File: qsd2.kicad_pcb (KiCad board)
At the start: 2 copper layers, 100 x 75 mm, 65 parts, among them J1 5-1814832-1, J2 5-1814832-1, J3 Conn_02x08_Odd_Even, J4 SJ-3524-SMT, U1 SN74LVC1G14DBV, U10 GALI-39, U2 SN74LVC1G14DBV, U3 SN74CBT3253, U4 SN74AC74PW, U5 AD8226ARZ-R7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

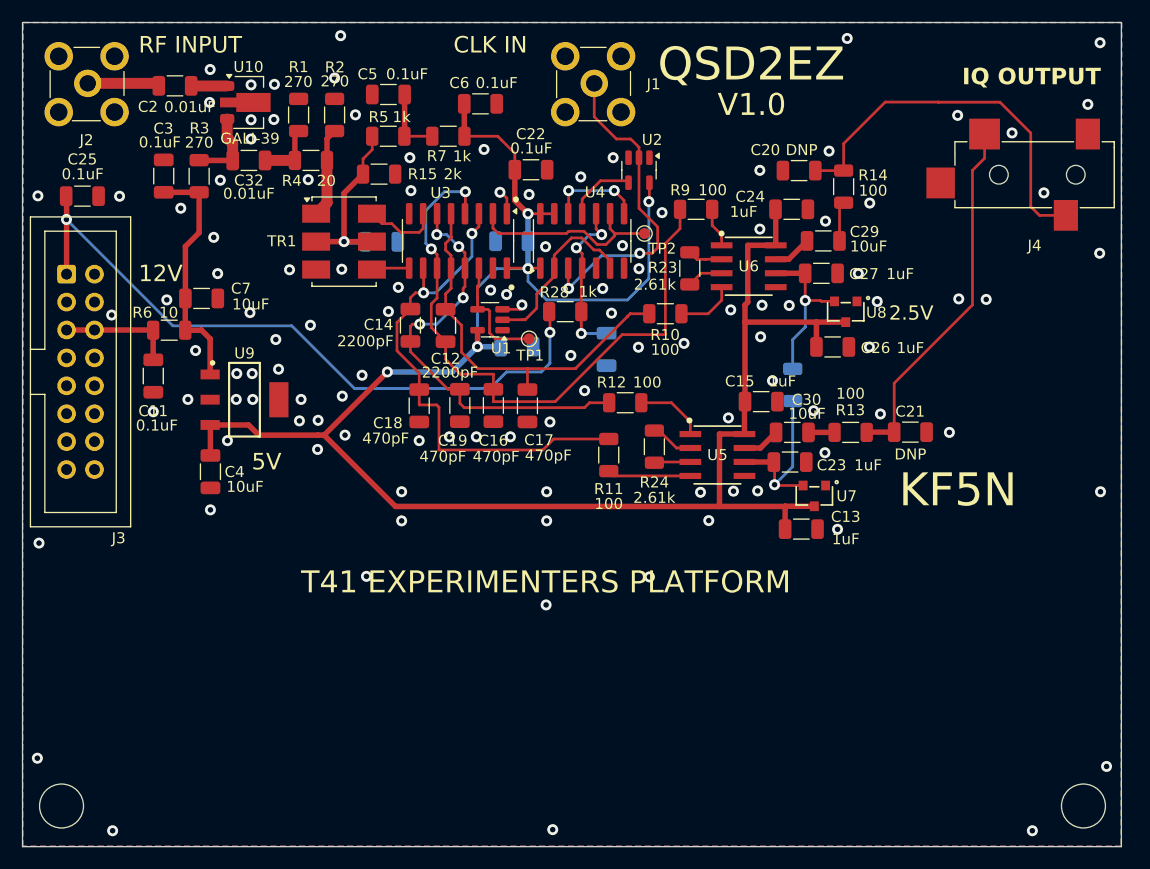
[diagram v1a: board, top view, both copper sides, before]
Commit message: Added 4 pin connector with 5V and I2C for Si5351 module.
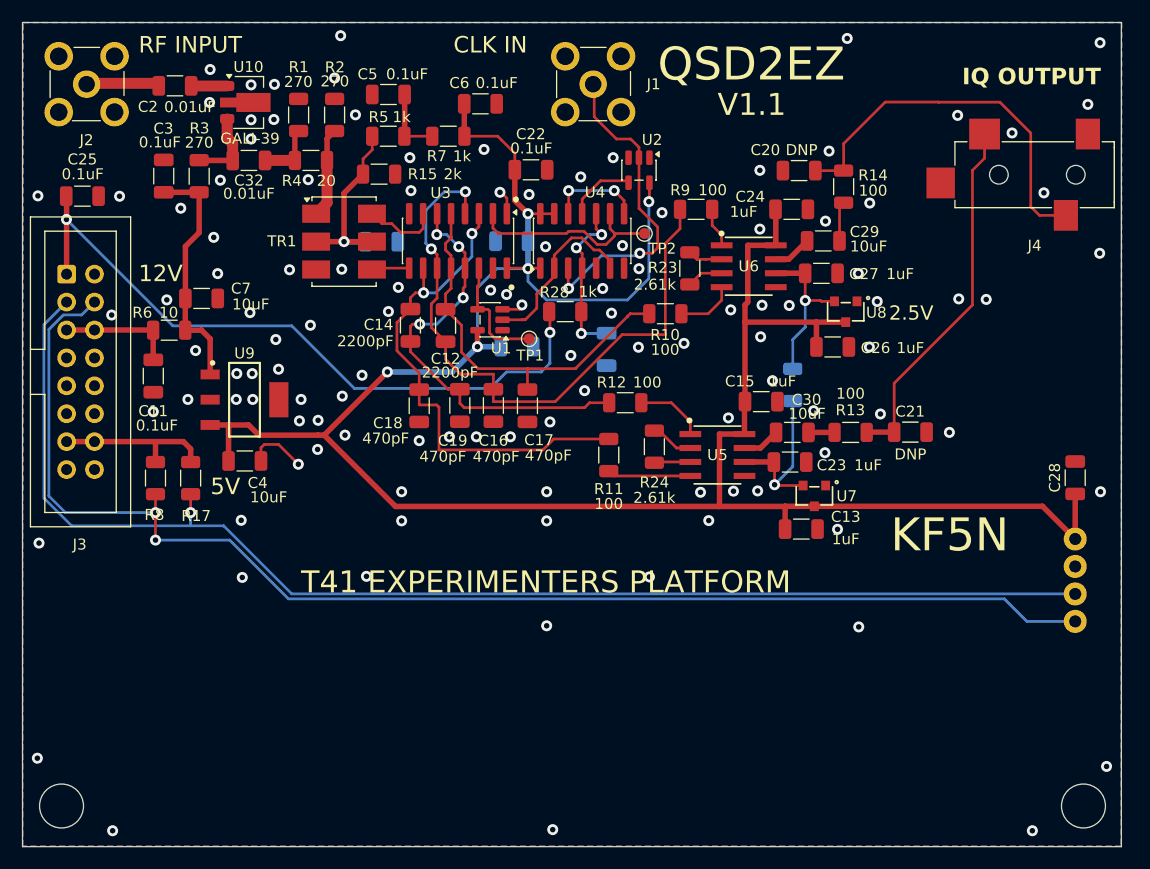
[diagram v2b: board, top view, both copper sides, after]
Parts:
- added C28: 0.1uF, Capacitor_SMD:C_1206_3216Metric, F.Cu at (195.0, 81.0)
- added J5: B4B-XH-A_LF__SN_, digikey-footprints:PinHeader_1x4_P2.5mm_Drill1.1mm, B.Cu at (195.0, 86.6)
- added R17: 4.7k, Resistor_SMD:R_1206_3216Metric, F.Cu at (114.5, 81.1)
- added R8: 4.7k, Resistor_SMD:R_1206_3216Metric, F.Cu at (111.3, 81.1)
- TR1: value ADT4-6T -> ADT4-6T+
- moved C4 3.27 mm to (119.4, 79.5), turned to 0 degrees
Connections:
- J3 pad 13: unconnected-(J3-Pin_13-Pad13) -> /3_3V
- J3 pad 14: unconnected-(J3-Pin_14-Pad14) -> /3_3V
- J3 pad 3: unconnected-(J3-Pin_3-Pad3) -> /SDA
- J3 pad 4: unconnected-(J3-Pin_4-Pad4) -> /SCL
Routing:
- net /SCL: track 0.00 -> 121.6 mm, vias 0 -> 2
- net /SDA: track 0.00 -> 119.0 mm, vias 0 -> 1
- net /5V_FILT: track 185.1 -> 214.7 mm
- net /3_3V: track 0.00 -> 14.6 mm
- net GND: track 4.62 -> 10.1 mm, vias 114 -> 116
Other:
- board text added: "TO SI5351"
- board text added: "V1.1"
- board text removed: "V1.0"

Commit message: Ready for fab QSD2EZ V1.1 May 21, 2026.
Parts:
- removed C13, C26: 1uF, Capacitor_SMD:C_1206_3216Metric
- removed U7, U8: AP2120N-2.5TRG1, AP2120N:SOT-23_DIO
- added C8: 0.1uF, Capacitor_SMD:C_1206_3216Metric, F.Cu at (160.1, 51.8)
- added R18: 4.7k, Resistor_SMD:R_1206_3216Metric, F.Cu at (179.1, 82.2)
- added R19: 4.7k, Resistor_SMD:R_1206_3216Metric, F.Cu at (168.9, 67.5)
- added TP3: TestPoint, Connector_PinHeader_2.54mm:PinHeader_1x01_P2.54mm_Vertical, F.Cu at (192.4, 64.8)
- added U11: SN74LVC1G14DBV, Package_TO_SOT_SMD:SOT-23-5, F.Cu at (155.3, 53.0)
- added U12: LM4040DBZ-2.5, Package_TO_SOT_SMD:SOT-23, F.Cu at (174.4, 81.1)
- added U13: LM4040DBZ-2.5, Package_TO_SOT_SMD:SOT-23, F.Cu at (173.8, 66.5)
- moved U2 5.50 mm to (157.7, 48.1)
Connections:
- J1 pad 2: /CLK1 -> Net-(J1-Pad2)
- U2 pad 2: /CLK1 -> Net-(J1-Pad2)
- U2 pad 4: /CLK2 -> /CLK1
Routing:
- net /REF_I: track 15.8 -> 25.3 mm
- net Net-(J1-Pad2): track 0.00 -> 7.74 mm
- net /CLK1: track 29.6 -> 23.7 mm
- net /5V_FILT: track 214.7 -> 209.7 mm
- net /REF_Q: track 14.6 -> 16.9 mm
- net GND: track 10.1 -> 12.0 mm, vias 116 -> 121
